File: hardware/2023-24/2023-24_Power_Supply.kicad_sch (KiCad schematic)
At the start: 37 parts, among them J1 USB_B_Micro, J2 Conn_01x02, U2 W25Q128JVS, U3 RP2040, Y1 ABLS-12.000MHZ-B4-T

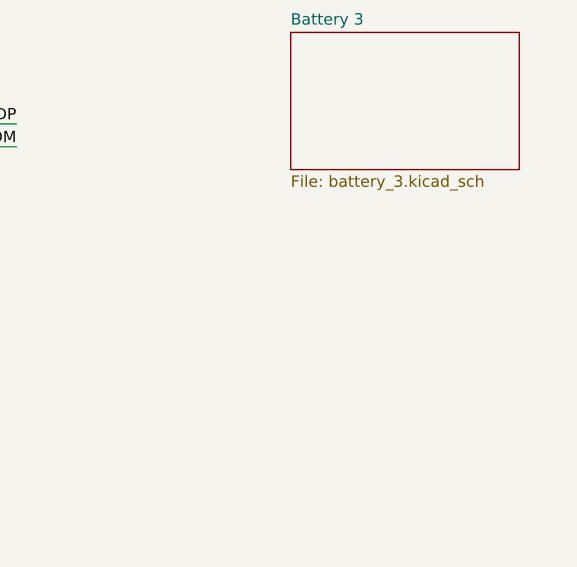
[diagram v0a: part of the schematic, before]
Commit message: regulator slot libraries
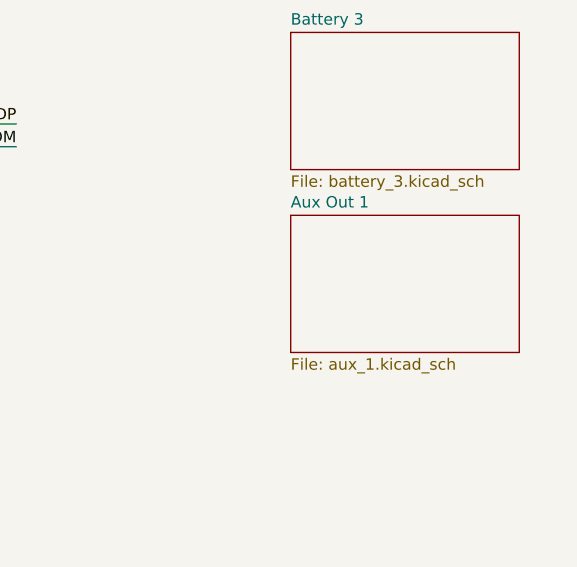
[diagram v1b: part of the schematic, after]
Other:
- added sheet Aux Out 1 (aux_1.kicad_sch)
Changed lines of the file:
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@@
+    )
+  )
+  (sheet (at 304.8 63.5) (size 25.4 15.24) (fields_autoplaced)
+    (stroke (width 0.1524) (type solid))
+    (fill (color 0 0 0 0.0000))
+    (property "Sheetname" "Aux Out 1" (at 304.8 62.7884 0)
+      (effects (font (size 1.27 1.27)) (justify left bottom))
+    )
+    (property "Sheetfile" "aux_1.kicad_sch" (at 304.8 79.3246 0)
+      (effects (font (size 1.27 1.27)) (justify left top))
+    )
+    (instances
+      (project "2023-24_Power_Supply"
+        (path "/9d08c113-56e0-4c7c-90b4-94c67f8b2e1a" (page "5"))
+      )
     )
   )

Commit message: Pushing for design review
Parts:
- added C17 (x2): 10u, Capacitor_SMD:C_0805_2012Metric, symbol Device:C
- added J1: Conn_02x03_Odd_Even, Connector_PinHeader_2.54mm:PinHeader_2x03_P2.54mm_Vertical_SMD, symbol Connector_Generic:Conn_02x03_Odd_Even
- added R3: 100k, Resistor_SMD:R_0402_1005Metric, symbol Device:R_Small_US
- added R6: 11.1k, Resistor_SMD:R_0402_1005Metric, symbol Device:R_Small_US
- added R7: 10k, Resistor_SMD:R_0603_1608Metric, symbol Device:R_Small_US
- added SW1: SW_MEC_5E, Button_Switch_SMD:SW_Push_1P1T_NO_Vertical_Wuerth_434133025816, symbol Switch:SW_MEC_5E
- added U3: NCP1117-3.3_SOT223, Package_TO_SOT_SMD:SOT-223-3_TabPin2, symbol Regulator_Linear:NCP1117-3.3_SOT223
- C14: renamed from C1; footprint (none) -> Capacitor_SMD:C_0402_1005Metric
- C16: renamed from C2; value ~ -> 910p; footprint (none) -> Capacitor_SMD:C_0402_1005Metric; Manufacturer (none) -> Kemet
- L1: value 15u -> 39u; footprint (none) -> Inductor_SMD:L_12x12mm_H6mm; MPN (none) -> MSS1260-393MLD
- R1: renamed from R3; footprint (none) -> Resistor_SMD:R_0402_1005Metric
- R2: renamed from R4; footprint (none) -> Resistor_SMD:R_0402_1005Metric
- R2: value DNF -> DNP
- R4: renamed from R1; value ~ -> 3.3M; footprint (none) -> Resistor_SMD:R_0402_1005Metric; Manufacturer (none) -> Vishay
- R5: renamed from R2; value ~ -> 453k; footprint (none) -> Resistor_SMD:R_0402_1005Metric; Manufacturer (none) -> Vishay
- U1: renamed from U2; value ~ -> MAX17502G
- U3: footprint RP2040_minimal:RP2040-QFN-56 -> Package_DFN_QFN:QFN-56-1EP_7x7mm_P0.4mm_EP3.2x3.2mm_ThermalVias
- renumbered C4 to C12, C3 to C13, J1 to J2
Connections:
- net +1V1: now also C6.1, C7.1
- net +3V3: now also C17.1, J1.3 (Pin_3), R7.1, U3.2 (VO); no longer C12.2 (-), C17.1, L1.2, U1.5 (FB/VO)
- net GND: now also C17.2, C17.2, J1.4 (Pin_4), R6.2, SW1.1, SW1.2, U3.1 (GND)
- net +9V_LX: now reaches L1.1, U1.10 (LX)
- net PGD_B2: now reaches U3.11 (GPIO8)
- net EN_B2: now reaches U3.12 (GPIO9)
- net PGD_B1: now reaches U3.13 (GPIO10)
- net EN_B1: now reaches U3.14 (GPIO11)
- net UART0_TX: now reaches U3.2 (GPIO0)
- net UART0_TX: now also J1.1 (Pin_1)
- net SWCLK: now reaches U3.24 (SWCLK)
- net SWCLK: now also J1.6 (Pin_6)
- net SWD: now reaches U3.25 (SWD)
- net SWD: now also J1.2 (Pin_2)
- net at U3.26 (RUN): now also R7.2, SW1.3 (K), SW1.4 (A)
- net ADC1_RDY: now reaches U3.29 (GPIO18)
- net UART0_RX: now reaches U3.3 (GPIO1)
- net UART0_RX: now also J1.5 (Pin_5)
- net ADC2_RDY: now reaches U3.30 (GPIO19)
- net PGD_AUX1: now reaches U3.31 (GPIO20)
- net EN_AUX_1: now reaches U3.32 (GPIO21)
- net PGD_AUX2: now reaches U3.34 (GPIO22)
- net EN_AUX_2: now reaches U3.35 (GPIO23)
- net PGD_AUX3: now reaches U3.36 (GPIO24)
- net EN_AUX_3: now reaches U3.37 (GPIO25)
- net I2C1_SDA: now reaches U3.38 (GPIO26_ADC0)
- net I2C1_SCL: now reaches U3.39 (GPIO27_ADC1)
- net I2C0_SDA: now reaches U3.6 (GPIO4)
- net I2C0_SCL: now reaches U3.7 (GPIO5)
- net PGD_B3: now reaches U3.8 (GPIO6)
- net EN_B3: now reaches U3.9 (GPIO7)
- net USB_DM renamed USB_D_N
- net USB_DP renamed USB_D_P
- new net: R3.2, R6.1, U1.5 (FB/VO)
- new net +9V: C12.2 (-), C17.1, C17.1, L1.2, R3.1, U3.3 (VI)
- no-connect marks 1 -> 2
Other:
- removed sheet Aux Out 1
- removed sheet Battery 1
- removed sheet Battery 2
- removed sheet Battery 3
- added sheet Aux Outputs (aux_outputs.kicad_sch)
- added sheet Battery Switching (battery_inputs.kicad_sch)
- note added: "Make sure C8 is close to pin 44 of RP2040"
- note added: "Make sure C9 is close to pin 45 of RP2040"
- note added: "Power"
- note added: "USB"
- note removed: "Make sure C10 is close to pin 44 of RP2040"
- note removed: "Make sure C8 is close to pin 45 of RP2040"
- moved on the sheet: C10, C11, C12, C13, C14, C15, C16, C17, C2, C3, C5, C6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

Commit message: Hardware ready for design review
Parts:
- removed C10, C8: 1u, Capacitor_SMD:C_0402_1005Metric, symbol Device:C
- removed C11, C12, C13, C14, C15, C16, C5, C6, C7, C9: 100n, Capacitor_SMD:C_0402_1005Metric, symbol Device:C
- removed C12, C13: 2.2u, Capacitor_SMD:C_1210_3225Metric, symbol PCM_Generic-50:C,IEC
- removed C14: 1u, Capacitor_SMD:C_0402_1005Metric, symbol PCM_Generic-50:C,IEC
- removed C16: 910p, Capacitor_SMD:C_0402_1005Metric, symbol PCM_Generic-50:C,IEC
- removed C17 (x3): 10u, Capacitor_SMD:C_0805_2012Metric, symbol Device:C
- removed C2, C3: 27p, Capacitor_SMD:C_0402_1005Metric, symbol Device:C
- removed D1, D2, D3, D4: PMEG10030ELPX, Diode_SMD:D_SOD-128, symbol Device:D_Schottky
- removed J1: Conn_02x03_Odd_Even, Connector_PinHeader_2.54mm:PinHeader_2x03_P2.54mm_Vertical_SMD, symbol Connector_Generic:Conn_02x03_Odd_Even
- removed J2: USB_B_Micro, Connector_USB:USB_Micro-B_Wuerth_629105150521_CircularHoles, symbol Connector:USB_B_Micro
- removed J2: Conn_01x02, Connector_PinHeader_2.54mm:PinHeader_1x02_P2.54mm_Vertical, symbol Connector_Generic:Conn_01x02
- removed L1: 39u, Inductor_SMD:L_12x12mm_H6mm, symbol Device:L
- removed R1, R5: 1k, Capacitor_SMD:C_0402_1005Metric, symbol Device:R
- removed R1, R2: 27, Resistor_SMD:R_0402_1005Metric, symbol Device:R_Small_US
- removed R2: DNP, Capacitor_SMD:C_0402_1005Metric, symbol Device:R
- removed R3: 100k, Resistor_SMD:R_0402_1005Metric, symbol Device:R_Small_US
- removed R4: 3.3M, Resistor_SMD:R_0402_1005Metric, symbol Device:R_Small_US
- removed R5: 453k, Resistor_SMD:R_0402_1005Metric, symbol Device:R_Small_US
- removed R6: 11.1k, Resistor_SMD:R_0402_1005Metric, symbol Device:R_Small_US
- removed R7: 10k, Resistor_SMD:R_0603_1608Metric, symbol Device:R_Small_US
- removed SW1: SW_MEC_5E, Button_Switch_SMD:SW_Push_1P1T_NO_Vertical_Wuerth_434133025816, symbol Switch:SW_MEC_5E
- removed U1: MAX17502G, Maxim:TDFN, symbol Maxim:MAX17502_TDFN
- removed U2: W25Q128JVS, Package_SO:SOIC-8_5.23x5.23mm_P1.27mm, symbol RP2040_minimal-rescue:W25Q128JVS-Memory_Flash
- removed U3: NCP1117-3.3_SOT223, Package_TO_SOT_SMD:SOT-223-3_TabPin2, symbol Regulator_Linear:NCP1117-3.3_SOT223
- removed U3: RP2040, Package_DFN_QFN:QFN-56-1EP_7x7mm_P0.4mm_EP3.2x3.2mm_ThermalVias, symbol MCU_RaspberryPi_RP2040:RP2040
- removed Y1: ABLS-12.000MHZ-B4-T, Crystal:Crystal_SMD_Abracon_ABM8G-4Pin_3.2x2.5mm, symbol Device:Crystal
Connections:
- no-connect marks 2 -> 0
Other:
- note removed: "60V MAX"
- note removed: "Crystal"
- note removed: "Flash"
- note removed: "Make sure C8 is close to pin 44 of RP2040"
- note removed: "Make sure C9 is close to pin 45 of RP2040"
- note removed: "Power"
- note removed: "Tie together GND and GND1 with a single connection"
- note removed: "USB"
